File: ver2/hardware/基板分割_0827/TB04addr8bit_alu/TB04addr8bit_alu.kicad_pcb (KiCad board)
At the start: 2 copper layers, 130 x 150 mm, 102 parts, among them IC201 74HC161N, IC202 74HC161N, IC203 74HC161N, IC204 74HC161N, IC301 74HC161N, IC302 74HC161N, IC303 74HC161N, IC304 74HC161N, J1602 Screw_Terminal_01x02, J2 Conn_02x20_Odd_Even, J3 Conn_02x10_Odd_Even, J601 Conn_02x05_Odd_Even, U102 74HC138, U201 74HC253, U202 74HC253, U203 74HC253, U204 74HC253, U301 74HC253, U302 74HC253, U303 74HC253, U304 74HC253, U402 74HC253, U403 74HC253, U405 74HC253, U406 74HC253, U603 28C256, U605 74HC74, U702 74HC273, U704 28C256

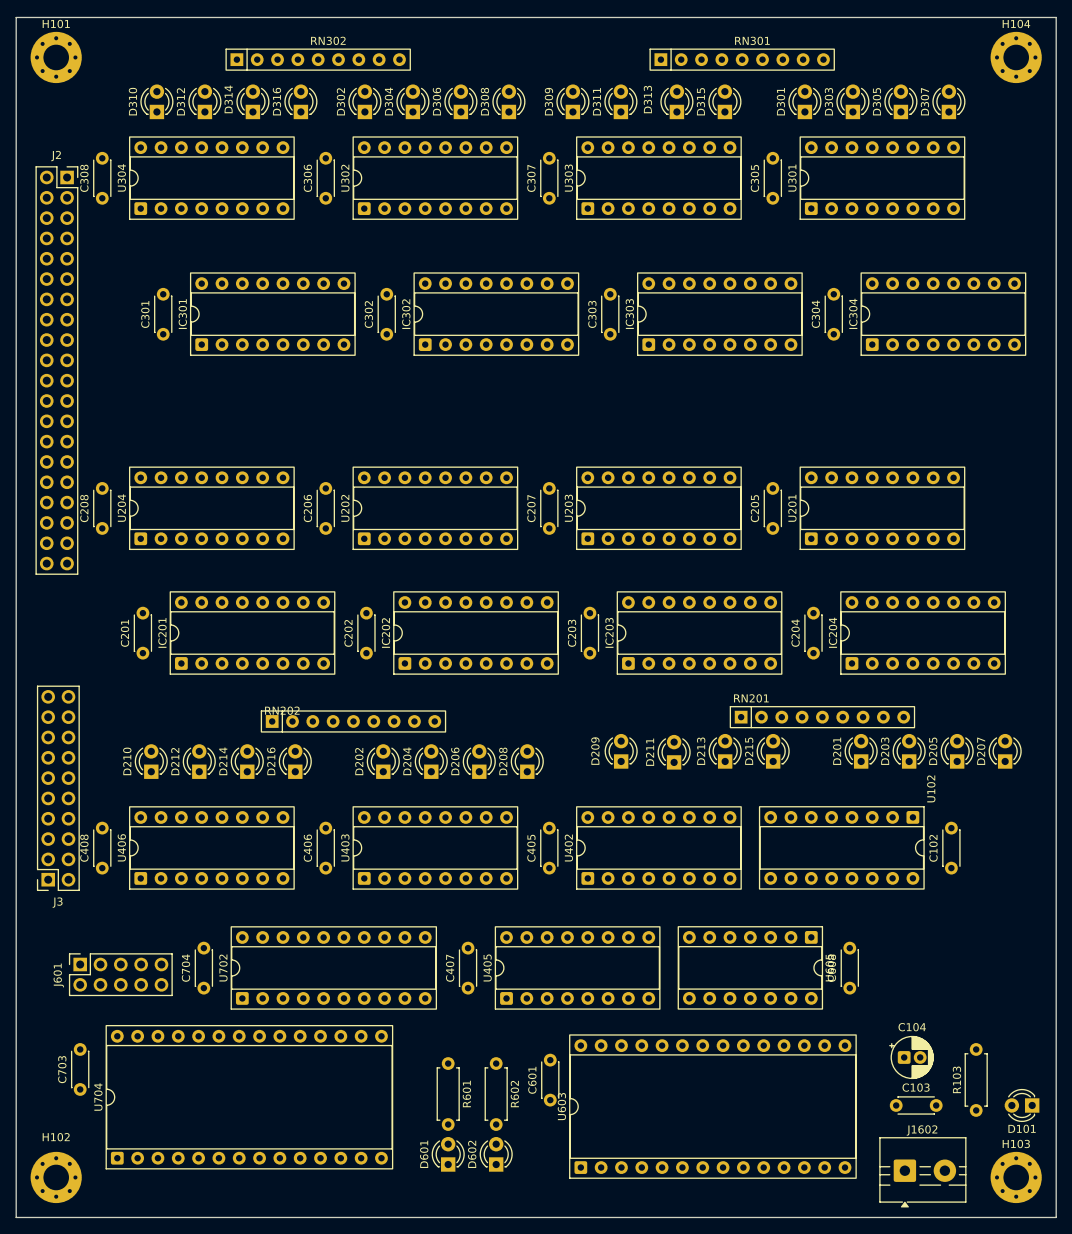
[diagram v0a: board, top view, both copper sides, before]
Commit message: ver2: 演算板の配線に着手(1434本・ビア209・必要接続の61%)
クリアランス違反0。GNDベタは未フィル。
DRC13件は配線途中のtrack_dangling 6とシルク7のみ。

Co-Authored-By: Claude Opus 5 <noreply@anthropic.com>
Claude-Session: https://claude.ai/code/session_01DiVc35doy1hdbtvPnQtG7V
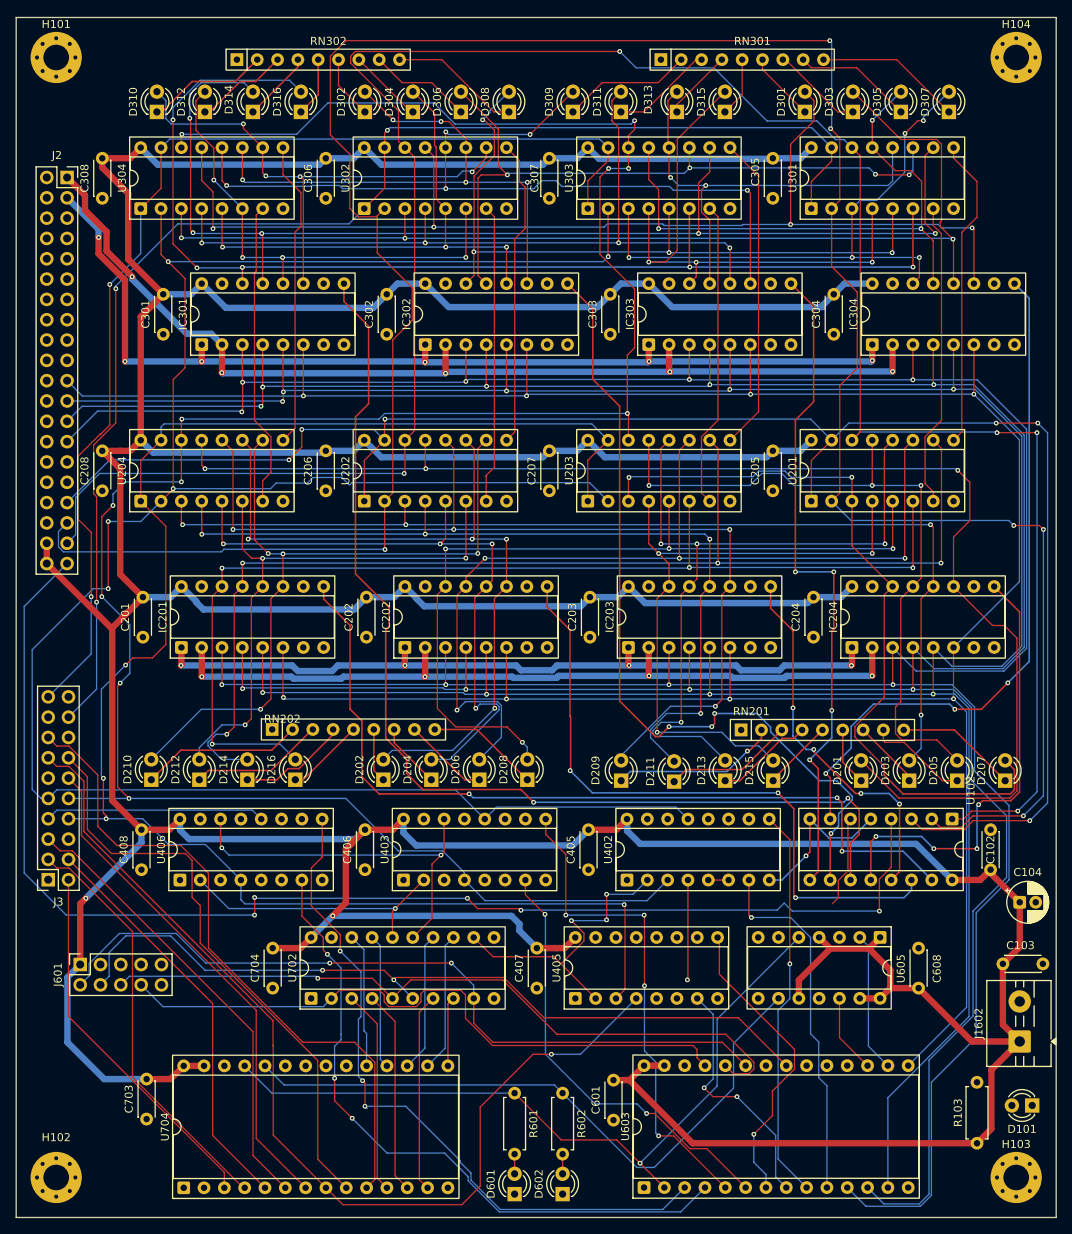
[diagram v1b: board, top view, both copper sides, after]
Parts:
- moved C104 24.2 mm to (225.4, 160.6)
- moved C103 22.2 mm to (223.3, 168.3)
- moved J1602 21.6 mm to (225.4, 178.0), turned to 90 degrees
- moved D601 9.09 mm to (162.3, 197.1)
- moved D602 9.09 mm to (168.3, 197.1)
- moved R601 9.09 mm to (162.3, 184.5)
- moved R602 9.09 mm to (168.3, 184.5)
- moved C703 9.09 mm to (116.3, 187.7)
- moved U704 9.09 mm to (120.9, 196.3)
- moved C407 8.60 mm to (165.1, 171.3)
- moved C608 8.60 mm to (212.8, 171.3)
- moved U605 8.60 mm to (208.0, 165.0)
- moved C704 8.60 mm to (132.1, 171.3)
- moved U405 8.60 mm to (169.9, 172.6)
- moved U702 8.60 mm to (136.9, 172.6)
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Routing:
- net VDD: track 0.00 -> 848.3 mm, vias 0 -> 2
- net DI0: track 0.00 -> 385.4 mm, vias 0 -> 9
- net DI1: track 0.00 -> 377.6 mm, vias 0 -> 9
- net DI2: track 0.00 -> 361.9 mm, vias 0 -> 9
- net DI3: track 0.00 -> 336.0 mm, vias 0 -> 8
- net sel_a1: track 0.00 -> 316.6 mm, vias 0 -> 6
- net OPR4: track 0.00 -> 302.8 mm, vias 0 -> 11
- net sel_a0: track 0.00 -> 290.3 mm, vias 0 -> 5
- net OPR5: track 0.00 -> 288.7 mm, vias 0 -> 5
- net CLK_CPU: track 0.00 -> 227.4 mm, vias 0 -> 9
- net ~{RST}: track 0.00 -> 219.9 mm, vias 0 -> 10
- net sel_a2: track 0.00 -> 215.9 mm, vias 0 -> 6
- net OPR6: track 0.00 -> 209.5 mm, vias 0 -> 4
- net /RS00/I1b3: track 0.00 -> 169.1 mm, vias 0 -> 3
- net ~{Ena_RS01}: track 0.00 -> 168.1 mm, vias 0 -> 3
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
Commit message: ver2: 演算板のDRC電気的違反をゼロに(20件→シルク9件のみ)
・OPR6のビアを0.15mm移動しクリアランス0.125→0.275mmに
・OPR0の片面ビアは配線途中だったのでF.Cu 46.2mmで本線に接続(ビア追加0)
・行き止まり8本(0.03〜0.42mmの削り残し)を削除
・EXEの引きかけをJ2.7まで接続(170.8mm・ビア3)
検証＝DRC 20→9(すべてシルク)・parityはHEADと項目一致・パッド署名の変化0・
未配線159→156(残156＝GND126＋信号30)。トラック1835→1854/ビア284→286。

Co-Authored-By: Claude Opus 5 <noreply@anthropic.com>
Claude-Session: https://claude.ai/code/session_01FHQyZznjPPN9g6quxMNLGo
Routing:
- net EXE: track 11.6 -> 182.4 mm, vias 0 -> 1
- net OPR0: track 95.5 -> 141.7 mm, vias 1 -> 2
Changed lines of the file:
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@@
 	)
 	(segment
-		(start 143.9 186.4)
-		(end 143.6 186.1)
-		(width 0.15)
-		(layer "B.Cu")
-		(net "alu_b3")
-	)
-	(segment
 		(start 135.71 162.31972)
 		(end 138.385 164.99472)
@@
 	(segment
 		(start 194.529569 184.2)
-		(end 194.5 184.2)
-		(width 0.15)
-		(layer "F.Cu")
-		(net "alu_a3")
-	)
-	(segment
-		(start 194.529569 184.2)
 		(end 194.529569 187.270431)
 		(width 0.15)
@@
 	)
 	(segment
-		(start 190.22 174.98)
-		(end 190.27 175.03)
-		(width 0.15)
-		(layer "F.Cu")
-		(net "alu_code2")
-	)
-	(segment
 		(start 165.954264 175.03)
 		(end 160.924264 170)
@@
 	)
 	(segment
-		(start 176 160.9)
+		(start 176 161.05)
 		(end 176.1 161)
 		(width 0.15)
@@
 	)
 	(via
-		(at 176 160.9)
+		(at 176 161.05)
 		(size 0.6)
 		(drill 0.3)
@@
 	(segment
 		(start 175.9 160.8)
-		(end 176 160.9)
+		(end 176 161.05)
 		(width 0.15)
 		(layer "B.Cu")
@@
 		(net "/RS00/I0a3")
 	)
-	(segment
-		(start 207.970431 135.5)
-		(end 207.885215 135.585215)
-		(width 0.15)
-		(layer "F.Cu")
-		(net "/RS00/I0a3")
-	)
 	(via
 		(at 204.456076 107.477821)
@@
 	)
 	(segment
-		(start 208.545 103.845)
-		(end 208.525 103.865)
-		(width 0.15)
-		(layer "F.Cu")
-		(net "/RS00/I0b2")
-	)
-	(segment
 		(start 185.1 120.18)
 		(end 185.1 115.8)
@@
 	)
 	(segment
+		(start 181.4 173.7)
+		(end 181.2 173.9)
+		(width 0.15)
+		(layer "F.Cu")
+		(net "OPR0")
+	)
+	(segment
 		(start 144.825 195.264775)
 		(end 144.825 180.625206)
@@
 	)
 	(segment
+		(start 182.6 170.3)
+		(end 181.4 171.5)
+		(width 0.15)
+		(layer "F.Cu")
+		(net "OPR0")
+	)
+	(segment
 		(start 142.299794 178.1)
 		(end 135.824264 178.1)
@@
 	)
 	(segment
+		(start 165.7 173.9)
+		(end 165.5 173.7)
+		(width 0.15)
+		(layer "F.Cu")
+		(net "OPR0")
+	)
+	(segment
 		(start 105.075 141.075)
 		(end 104 140)
@@
 	)
 	(segment
+		(start 144.5 182.5)
+		(end 144.8 182.5)
+		(width 0.15)
+		(layer "F.Cu")
+		(net "OPR0")
+	)
+	(segment
+		(start 181.2 173.9)
+		(end 165.7 173.9)
+		(width 0.15)
+		(layer "F.Cu")
+		(net "OPR0")
+	)
+	(segment
 		(start 106.59528 141.075)
 		(end 105.075 141.075)
@@
 	)
 	(segment
+		(start 181.4 171.5)
+		(end 181.4 173.7)
+		(width 0.15)
+		(layer "F.Cu")
+		(net "OPR0")
+	)
+	(segment
 		(start 120.563833 153.5)
 		(end 112.6 153.5)
@@
 		(net "OPR0")
 	)
+	(segment
+		(start 183.9 170.3)
+		(end 182.6 170.3)
+		(width 0.15)
+		(layer "F.Cu")
+		(net "OPR0")
+	)
+	(via
+		(at 165.5 173.7)
+		(size 0.6)
+		(drill 0.3)
+		(layers "F.Cu" "B.Cu")
+		(net "OPR0")
+	)
 	(via
-		(at 183.9 170.3)
+		(at 144.5 182.5)
 		(size 0.6)
 		(drill 0.3)
@@
 	)
 	(segment
+		(start 165.5 173.7)
+		(end 156.7 182.5)
+		(width 0.15)
+		(layer "B.Cu")
+		(net "OPR0")
+	)
+	(segment
+		(start 156.7 182.5)
+		(end 144.5 182.5)
+		(width 0.15)
+		(layer "B.Cu")
+		(net "OPR0")
+	)
+	(segment
 		(start 214.63 109.287537)
 		(end 214.63 110.46)
@@
 	)
 	(segment
-		(start 199.65 70.25)
-		(end 199.6 70.3)
-		(width 0.15)
-		(layer "B.Cu")
-		(net "~{Ena_RS01}")
-	)
-	(segment
 		(start 106.54 137.46)
 		(end 110.05 133.95)
@@
 	(segment
 		(start 154.665 103.835)
-		(end 154.7 103.87)
-		(width 0.15)
-		(layer "F.Cu")
-		(net "/RS00/I1b2")
-	)
-	(segment
-		(start 154.665 103.835)
 		(end 154.665 104.865)
 		(width 0.15)
@@
 	)
 	(segment
-		(start 218.5 151.515)
-		(end 218.585 151.515)
-		(width 0.15)
-		(layer "F.Cu")
-		(net "sel_a2")
-	)
-	(segment
 		(start 213.235 151.515)
 		(end 218.5 151.515)
@@
 	)
 	(segment
+		(start 199.1 166.1)
+		(end 199.1 166.8)
+		(width 0.15)
+		(layer "F.Cu")
+		(net "EXE")
+	)
+	(segment
+		(start 182.7 149.1)
+		(end 177 143.4)
+		(width 0.15)
+		(layer "F.Cu")
+		(net "EXE")
+	)
+	(segment
+		(start 177 143.4)
+		(end 177 141.6)
+		(width 0.15)
+		(layer "F.Cu")
+		(net "EXE")
+	)
+	(segment
+		(start 194.3 168.9)
+		(end 185.2 159.8)
+		(width 0.15)
+		(layer "F.Cu")
+		(net "EXE")
+	)
+	(segment
 		(start 203.965 156.685431)
 		(end 202.775 157.875431)
@@
 	)
 	(segment
+		(start 199.1 166.8)
+		(end 197 168.9)
+		(width 0.15)
+		(layer "F.Cu")
+		(net "EXE")
+	)
+	(segment
+		(start 199.1 163.7)
+		(end 199.1 166.1)
+		(width 0.15)
+		(layer "F.Cu")
+		(net "EXE")
+	)
+	(segment
+		(start 185.2 153.8)
+		(end 182.7 151.3)
+		(width 0.15)
+		(layer "F.Cu")
+		(net "EXE")
+	)
+	(segment
+		(start 182.7 151.3)
+		(end 182.7 149.1)
+		(width 0.15)
+		(layer "F.Cu")
+		(net "EXE")
+	)
+	(segment
+		(start 197 168.9)
+		(end 194.3 168.9)
+		(width 0.15)
+		(layer "F.Cu")
+		(net "EXE")
+	)
+	(segment
+		(start 185.2 159.8)
+		(end 185.2 153.8)
+		(width 0.15)
+		(layer "F.Cu")
+		(net "EXE")
+	)
+	(segment
+		(start 170.2 134.8)
+		(end 170.2 92.3)
+		(width 0.15)
+		(layer "F.Cu")
+		(net "EXE")
+	)
+	(segment
 		(start 204.29 150.19)
 		(end 203.965 150.515)
@@
 		(net "EXE")
 	)
+	(segment
+		(start 202 160.8)
+		(end 199.1 163.7)
+		(width 0.15)
+		(layer "F.Cu")
+		(net "EXE")
+	)
+	(segment
+		(start 170.2 92.3)
+		(end 170.4 92.1)
+		(width 0.15)
+		(layer "F.Cu")
+		(net "EXE")
+	)
+	(segment
+		(start 177 141.6)
+		(end 170.2 134.8)
+		(width 0.15)
+		(layer "F.Cu")
+		(net "EXE")
+	)
+	(via
+		(at 170.4 92.1)
+		(size 0.6)
+		(drill 0.3)
+		(layers "F.Cu" "B.Cu")
+		(net "EXE")
+	)
+	(segment
+		(start 118.5 92.1)
+		(end 108.3 81.9)
+		(width 0.15)
+		(layer "B.Cu")
+		(net "EXE")
+	)
+	(segment
+		(start 170.4 92.1)
+		(end 118.5 92.1)
+		(width 0.15)
+		(layer "B.Cu")
+		(net "EXE")
+	)
+	(segment
+		(start 108.3 79.7)
+		(end 106.5 77.9)
+		(width 0.15)
+		(layer "B.Cu")
+		(net "EXE")
+	)
+	(segment
+		(start 108.3 81.9)
+		(end 108.3 79.7)
+		(width 0.15)
+		(layer "B.Cu")
+		(net "EXE")
+	)
